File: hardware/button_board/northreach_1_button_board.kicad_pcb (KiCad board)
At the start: 2 copper layers, 41 x 96 mm, 18 parts, among them J1 Conn_01x20, SW10 Fn_1, SW11 Fn_2, SW12 Fn_3, SW13 Fn_4, SW3 Left, SW4 Right, SW5 Up, SW6 Vol_Up, SW7 Down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

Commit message: pcb: button board: labels and copyright lol
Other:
- board text added: "NorthReach 1 - Button Board v1 - Designed on Jan. 8th 2025 in Athens, Greece Stratos Thivaios (C) 2025"
- board text added: "NorthReach 1 - v1 Stratos Thivaios (C) 2025"
- board text added: "github.com/sthivaios/northreach_1 CERN Open Hardware Licence Version 2 - CERN-OHL-S"
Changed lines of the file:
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@@
 		(layer "Edge.Cuts")
 	)
-	(segment
-		(start 132.85 131.85)
-		(end 141.85 131.85)
-		(width 0.15)
-		(layer "F.Cu")
-		(net 1)
-	)
-	(segment
-		(start 141.85 131.85)
+	(gr_text "NorthReach 1 - v1\nStratos Thivaios (C) 2025"
+		(at 148 50 0)
+		(layer "F.SilkS")
+		(effects
+			(font
+				(size 0.8 0.8)
+				(thickness 0.2)
+				(bold yes)
+			)
+			(justify bottom)
+		)
+	)
+	(gr_text "github.com/sthivaios/northreach_1\nCERN Open Hardware Licence Version 2 - CERN-OHL-S"
+		(at 148 140.5 0)
+		(layer "B.SilkS")
+		(effects
+			(font
+				(size 0.8 0.8)
+				(thickness 0.1)
+			)
+			(justify bottom mirror)
+		)
+	)
+	(gr_text "NorthReach 1 - Button Board\nv1 - Designed on Jan. 8th 2025\nin Athens, Greece\nStratos Thivaios (C) 2025"
+		(at 148 134 0)
+		(layer "B.SilkS")
+		(effects
+			(font
+				(size 0.9 0.9)
+				(thickness 0.1)
+			)
+			(justify bottom mirror)
+		)
+	)
+	(segment
+		(start 141.25 131.25)
 		(end 144.15 134.15)
+		(width 0.15)
+		(layer "F.Cu")
+		(net 1)
+	)
+	(segment
+		(start 130.35 79.65)
+		(end 129.05 79.65)
 		(width 0.15)
 		(layer "F.Cu")
@@
 	)
 	(segment
-		(start 128.1 80.6)
-		(end 128.1 127.1)
-		(width 0.15)
-		(layer "F.Cu")
-		(net 1)
-	)
-	(segment
-		(start 130.35 79.65)
-		(end 129.05 79.65)
-		(width 0.15)
-		(layer "F.Cu")
-		(net 1)
-	)
-	(segment
-		(start 128.1 127.1)
-		(end 132.85 131.85)
+		(start 128.25 80.45)
+		(end 128.25 127.25)
 		(width 0.15)
 		(layer "F.Cu")
@@
 	(segment
 		(start 129.05 79.65)
-		(end 128.1 80.6)
+		(end 128.25 80.45)
+		(width 0.15)
+		(layer "F.Cu")
+		(net 1)
+	)
+	(segment
+		(start 132.25 131.25)
+		(end 141.25 131.25)
 		(width 0.15)
 		(layer "F.Cu")
@@
 		(start 130.35 79.65)
 		(end 133.9 79.65)
+		(width 0.15)
+		(layer "F.Cu")
+		(net 1)
+	)
+	(segment
+		(start 128.25 127.25)
+		(end 132.25 131.25)
 		(width 0.15)
 		(layer "F.Cu")
@@
 	)
 	(segment
+		(start 148.65 133.15)
+		(end 148.65 135.75)
+		(width 0.15)
+		(layer "F.Cu")
+		(net 16)
+	)
+	(segment
+		(start 133.6 117.35)
+		(end 132.35 118.6)
+		(width 0.15)
+		(layer "F.Cu")
+		(net 16)
+	)
+	(segment
+		(start 144.35 117.35)
+		(end 133.6 117.35)
+		(width 0.15)
+		(layer "F.Cu")
+		(net 16)
+	)
+	(segment
+		(start 152.65 120.8)
+		(end 147.8 120.8)
+		(width 0.15)
+		(layer "F.Cu")
+		(net 16)
+	)
+	(segment
+		(start 132.35 118.6)
+		(end 132.35 126.35)
+		(width 0.15)
+		(layer "F.Cu")
+		(net 16)
+	)
+	(segment
 		(start 147.8 120.8)
 		(end 144.35 117.35)
@@
 	)
 	(segment
+		(start 132.35 126.35)
+		(end 134.35 128.35)
+		(width 0.15)
+		(layer "F.Cu")
+		(net 16)
+	)
+	(segment
+		(start 134.35 128.35)
+		(end 143.85 128.35)
+		(width 0.15)
+		(layer "F.Cu")
+		(net 16)
+	)
+	(segment
 		(start 143.85 128.35)
 		(end 148.65 133.15)
@@
 	)
 	(segment
-		(start 134.35 128.35)
-		(end 143.85 128.35)
-		(width 0.15)
-		(layer "F.Cu")
-		(net 16)
-	)
-	(segment
-		(start 148.65 133.15)
-		(end 148.65 135.75)
-		(width 0.15)
-		(layer "F.Cu")
-		(net 16)
-	)
-	(segment
-		(start 133.6 117.35)
-		(end 132.35 118.6)
-		(width 0.15)
-		(layer "F.Cu")
-		(net 16)
-	)
-	(segment
-		(start 152.65 120.8)
-		(end 147.8 120.8)
-		(width 0.15)
-		(layer "F.Cu")
-		(net 16)
-	)
-	(segment
-		(start 132.35 126.35)
-		(end 134.35 128.35)
-		(width 0.15)
-		(layer "F.Cu")
-		(net 16)
-	)
-	(segment
-		(start 144.35 117.35)
-		(end 133.6 117.35)
-		(width 0.15)
-		(layer "F.Cu")
-		(net 16)
-	)
-	(segment
 		(start 152.65 120.8)
 		(end 159.15 120.8)
 		(width 0.15)
 		(layer "F.Cu")
-		(net 16)
-	)
-	(segment
-		(start 132.35 118.6)
-		(end 132.35 126.35)
-		(width 0.15)
-		(layer "F.Cu")

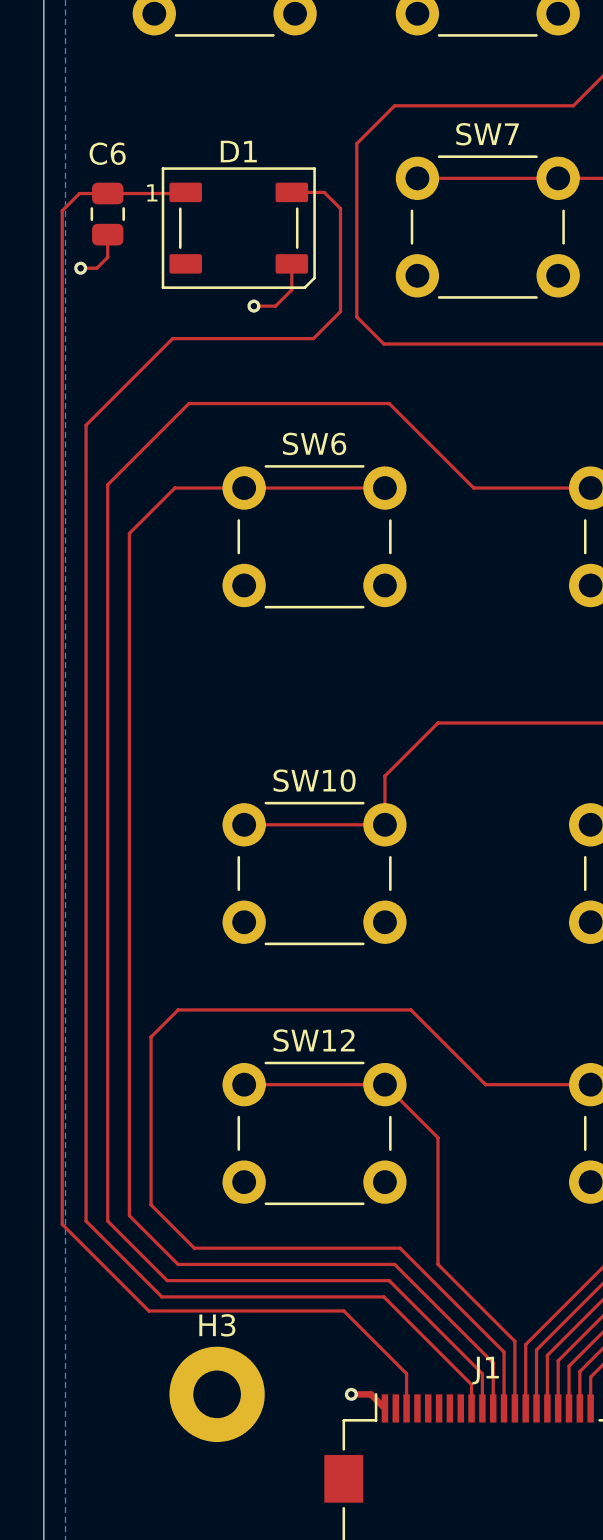
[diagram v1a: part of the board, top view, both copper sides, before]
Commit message: schematic_and_pcb: button board: remove led for now
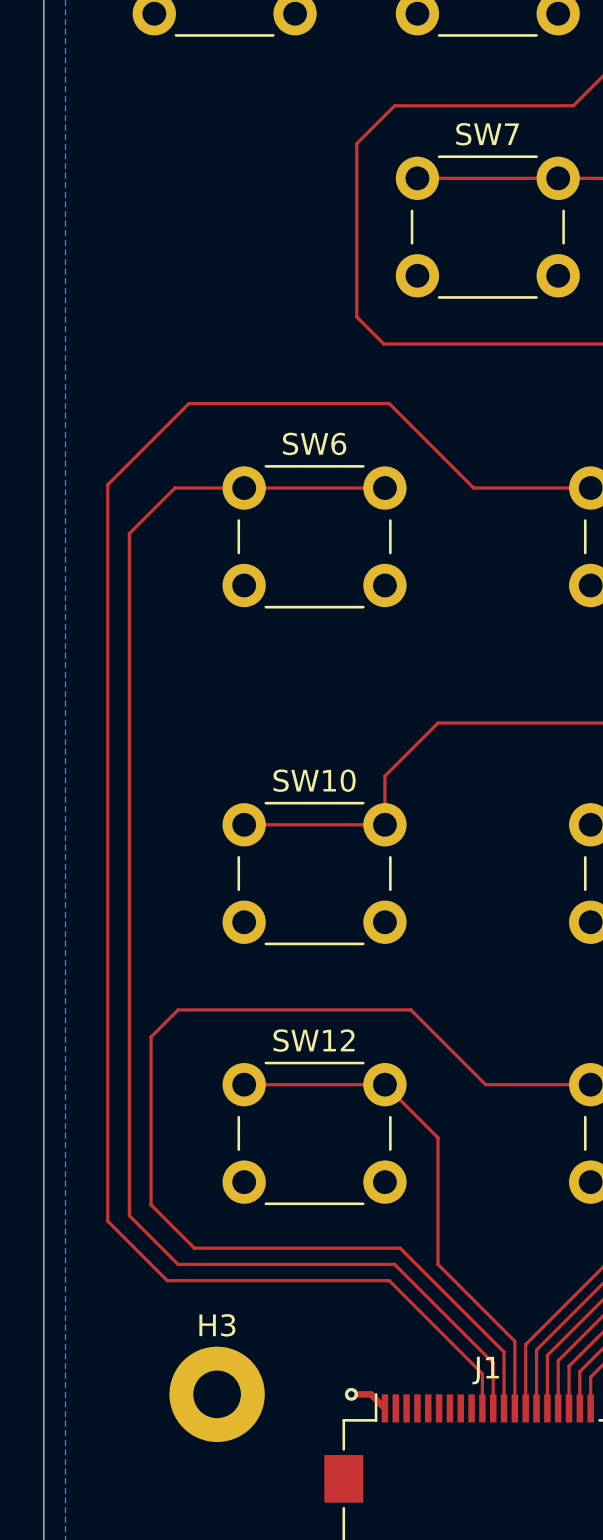
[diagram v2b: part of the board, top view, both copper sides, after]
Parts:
- removed C6: 0.1uF, Capacitor_SMD:C_0805_2012Metric
- removed D1: WS2812B, LED_SMD:LED_WS2812B_PLCC4_5.0x5.0mm_P3.2mm
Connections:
- J1 pad 9: STATUS_LED_DATA -> unconnected-(J1-Pin_9-Pad9)
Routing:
- net STATUS_LED_DATA: track 80.0 -> 0.00 mm
- net VBUS: track 73.2 -> 0.00 mm
- net GND: track 7.59 -> 1.82 mm, vias 3 -> 1
